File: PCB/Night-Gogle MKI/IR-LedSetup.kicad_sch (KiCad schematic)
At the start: 14 parts, among them U1 IRL540N

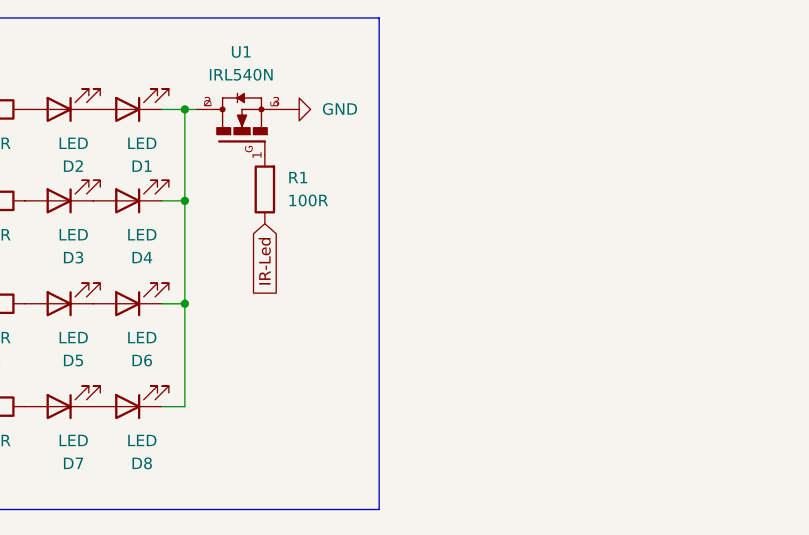
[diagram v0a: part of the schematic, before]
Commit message: pcb update
was created main board pcb + pice of IR_led
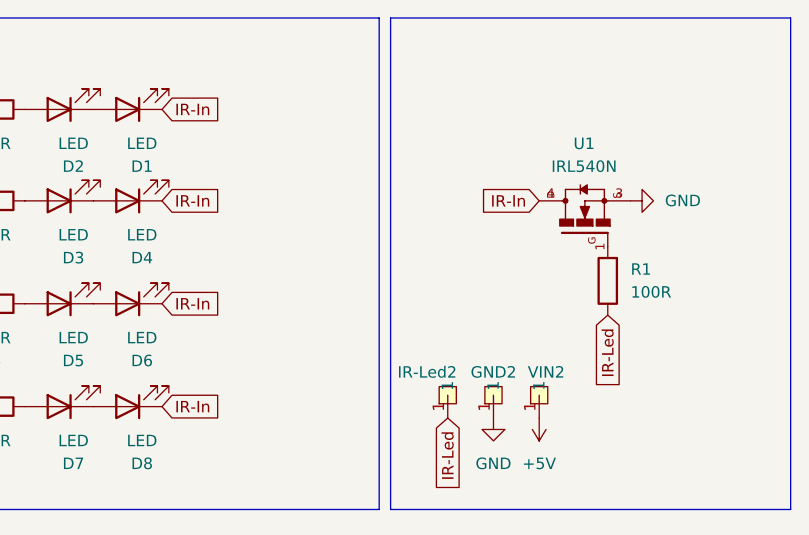
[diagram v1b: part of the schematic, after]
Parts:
- added GND2, IR-Led2, VIN2: ~, N-G_board:Pad-3.5mm, symbol N-G:Pad-3.5mm
- R1, R2, R3, R4, R5: footprint (none) -> Resistor_THT:R_Axial_DIN0411_L9.9mm_D3.6mm_P12.70mm_Horizontal
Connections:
- net +5V: now also VIN2.1
- net GND: now also GND2.1
- net IR-Led: now also IR-Led2.1
- net IR-In: now reaches D1.1 (K), D4.1 (K), D6.1 (K), D8.1 (K)
- net IR-In: now also U1.4; no longer U1.2
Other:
- moved on the sheet: R1

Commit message: pcb update
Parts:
- removed GND2: ~, N-G_board:Pad-3.5mm, symbol N-G:Pad-3.5mm
- removed R1: 100R, Resistor_THT:R_Axial_DIN0411_L9.9mm_D3.6mm_P12.70mm_Horizontal, symbol Device:R
- removed U1: IRL540N, N-G_board:TO254P1524X483-4N, symbol N-G:IRL540N
- R2, R3, R4, R5: footprint Resistor_THT:R_Axial_DIN0411_L9.9mm_D3.6mm_P12.70mm_Horizontal -> Resistor_SMD:R_1206_3216Metric_Pad1.30x1.75mm_HandSolder
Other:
- moved on the sheet: IR-Led2, VIN2

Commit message: gg
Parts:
- R2, R3, R4, R5: value 100R -> 160R
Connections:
- net IR-Led is gone; now on net IR-In: IR-Led2.1
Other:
- note added: "IR-Led setup"
- note removed: "Zapojení"
- moved on the sheet: D1, D2, D3, D4, D5, D6, D7, D8, IR-Led2, R2, R3, R4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
